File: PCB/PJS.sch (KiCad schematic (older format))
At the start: 22 parts

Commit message: Current Schematic and Footprints.
Pins between schematic and footprint are now mostly in alignment. The altimeter has a footprint, and JST connectors are to size.
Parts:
- removed S? (x4): LimitSwitch, PJS:LimitSwitch, symbol PJS:LimitSwitch
- removed X?: XT30-F_MotorConnector, PJS:XT30_Female_MotorConnector, symbol PJS:XT30-F_MotorConnector
- added S? (x7): JST_2Pin, symbol PJS:JST_2Pin
- added X? (x2): XT30-F_MotorConnector, PJS:XT30_Female_MotorConnector, symbol PJS:XT30-F_MotorConnector
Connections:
- net labels added: Door_BridgeAOut1, Door_BridgeAOut2, Door_DriverBOut1, Door_DriverBOut2, Door_RelayOut1, Door_RelayOut2, Link_DriverInA, Link_DriverInB, Link_DriverOutA, Link_DriverOutB, Link_DriverPWM, Relay_Signal
- net labels removed: LinkDriver_InA, LinkDriver_InB, LinkDriver_OutA, LinkDriver_OutB, LinkDriver_PWM, RelaySignal
- wire segments 68 -> 76
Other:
- moved on the sheet: C?, R?, X?

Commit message: 99% Complete Schematic and Footprints.
The only items on the schematic that are not complete are the switches, as the 5th switch needs to be defined and all of them should be renamed.

Some of the Teensy pins are not named properly either. Besides that, every component should be correctly associated with an accurate footprint.
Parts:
- removed A?: BMP388_AdafruitAltimeter, PJS:BMP388, symbol PJS:BMP388_AdafruitAltimeter
- removed A?: DRV8871_AuxMotorDriver, symbol PJS:DRV8871_AuxMotorDriver
- removed Q?: 2N2222_Transistor, symbol PJS:2N2222_Transistor
- removed X?: XT30-F_MotorConnector, PJS:XT30_Female_MotorConnector, symbol PJS:XT30-F_MotorConnector
- added A?: BMP388_Altimeter, PJS:BMP388_Altimeter, symbol PJS:BMP388_Altimeter
- added A? (x4): DRV8871_MotorDriver, PJS:DRV8871_MotorDriver, symbol PJS:DRV8871_MotorDriver
- added C? (x3): 47uF, PJS:EEE-1CA470SP_Capacitor, symbol PJS:CP
- added C? (x3): 0.1uF, PJS:CL05B104KO5NNNC_Capacitor, symbol PJS:C
- added Q?: MMBT222A_Transistor, PJS:MMBT2222A_Transistor, symbol PJS:MMBT222A_Transistor
- added R?: 30k, PJS:0402_Resistor, symbol PJS:R
- added R? (x2): 82k, PJS:0402_Resistor, symbol PJS:R
- added S?: JST_2Pin, symbol PJS:JST_2Pin
- added S?: JST_2Pin, PJS:JST_2Pin, symbol PJS:JST_2Pin
- A?: footprint PJS:TBS_Crossfire_RX -> PJS:TBS_Crossfire_RF_Receiver
- C?: footprint (none) -> PJS:EEE-1CA470SP_Capacitor
- C?: footprint (none) -> PJS:CL05B104KO5NNNC_Capacitor
- D?: footprint (none) -> PJS:1SS351-TB-E_Diode
- R?: footprint (none) -> PJS:0402_Resistor
- R?: footprint (none) -> PJS:MicroSD_Slot
- S? (x3): footprint (none) -> PJS:JST_2Pin
- VR?: footprint PJS:D24V22F5 -> PJS:D24V22F5_VoltageRegulator
- XM?: footprint PJS:microSD_HC_Molex_104031-0811 -> PJS:MicroSD_Slot
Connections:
- net labels added: Link_DriverIN1, Link_DriverIN2, Link_DriverOUT1, Link_DriverOUT2, LockA_DriverIN1, LockA_DriverIN2, LockA_DriverOUT1, LockA_DriverOUT2, LockA_DriverOut2, LockB_DriverIN1, LockB_DriverIN2, LockB_DriverOUT1, LockB_DriverOUT2, S3_UAS
- net labels removed: Door_BridgeAOut1, Door_BridgeAOut2, Door_DriverBOut1, Door_DriverBOut2
- wire segments 76 -> 109
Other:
- moved on the sheet: C?, D?, K?, R?, S?, X?

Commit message: library localization fixes
confuses library paths and missing files solved by including them within the realm of the github folder instead of local documents
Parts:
- A?: symbol PJS:Teensy4.0 -> PJS-rescue:Teensy4.0-PJS
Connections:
- net +5V: now also A?.~ (VUSB); no longer A?.T_VIN (VIN)
- net GND: no longer A?.GND
- net S3_UAS: now also A?.1 (1_TX1_CTX2_MISO1)
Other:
- moved on the sheet: BT?, J?, VR?, X?, XM?
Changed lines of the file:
@@
 L power:GND #PWR?
 U 1 1 5FF2ED77
-P 14200 2900
-F 0 "#PWR?" H 14200 2650 50  0001 C CNN
-F 1 "GND" V 14205 2772 50  0000 R CNN
-F 2 "" H 14200 2900 50  0001 C CNN
-F 3 "" H 14200 2900 50  0001 C CNN
-	1    14200 2900
+P 13800 2500
+F 0 "#PWR?" H 13800 2250 50  0001 C CNN
+F 1 "GND" V 13805 2372 50  0000 R CNN
+F 2 "" H 13800 2500 50  0001 C CNN
+F 3 "" H 13800 2500 50  0001 C CNN
+	1    13800 2500
 	0    1    1    0
 $EndComp
@@
 L power:+12V #PWR?
 U 1 1 5FF717BB
-P 12400 2200
-F 0 "#PWR?" H 12400 2050 50  0001 C CNN
-F 1 "+12V" V 12415 2328 50  0000 L CNN
-F 2 "" H 12400 2200 50  0001 C CNN
-F 3 "" H 12400 2200 50  0001 C CNN
-	1    12400 2200
+P 12000 1800
+F 0 "#PWR?" H 12000 1650 50  0001 C CNN
+F 1 "+12V" V 12015 1928 50  0000 L CNN
+F 2 "" H 12000 1800 50  0001 C CNN
+F 3 "" H 12000 1800 50  0001 C CNN
+	1    12000 1800
 	0    -1   -1   0
 $EndComp
@@
 L power:GND #PWR?
 U 1 1 5FF70E20
-P 13100 2150
-F 0 "#PWR?" H 13100 1900 50  0001 C CNN
-F 1 "GND" V 13105 2022 50  0000 R CNN
-F 2 "" H 13100 2150 50  0001 C CNN
-F 3 "" H 13100 2150 50  0001 C CNN
-	1    13100 2150
+P 12700 1750
+F 0 "#PWR?" H 12700 1500 50  0001 C CNN
+F 1 "GND" V 12705 1622 50  0000 R CNN
+F 2 "" H 12700 1750 50  0001 C CNN
+F 3 "" H 12700 1750 50  0001 C CNN
+	1    12700 1750
 	0    -1   -1   0
 $EndComp
@@
 L power:+5V #PWR?
 U 1 1 5FF7064D
-P 13100 2050
-F 0 "#PWR?" H 13100 1900 50  0001 C CNN
-F 1 "+5V" V 13115 2178 50  0000 L CNN
-F 2 "" H 13100 2050 50  0001 C CNN
-F 3 "" H 13100 2050 50  0001 C CNN
-	1    13100 2050
-	0    1    1    0
-$EndComp
-Text Label 13700 2700 0    50   ~ 0
+P 12700 1650
+F 0 "#PWR?" H 12700 1500 50  0001 C CNN
+F 1 "+5V" V 12715 1778 50  0000 L CNN
+F 2 "" H 12700 1650 50  0001 C CNN
+F 3 "" H 12700 1650 50  0001 C CNN
+	1    12700 1650
+	0    1    1    0
+$EndComp
+Text Label 13300 2300 0    50   ~ 0
 3.3V_Coin
 Wire Wire Line
-	14200 2700 13700 2700
+	13800 2300 13300 2300
 $Comp
 L power:GND #PWR?
 U 1 1 5FF2647A
-P 14100 2150
-F 0 "#PWR?" H 14100 1900 50  0001 C CNN
-F 1 "GND" V 14105 2022 50  0000 R CNN
-F 2 "" H 14100 2150 50  0001 C CNN
-F 3 "" H 14100 2150 50  0001 C CNN
-	1    14100 2150
+P 13700 1750
+F 0 "#PWR?" H 13700 1500 50  0001 C CNN
+F 1 "GND" V 13705 1622 50  0000 R CNN
+F 2 "" H 13700 1750 50  0001 C CNN
+F 3 "" H 13700 1750 50  0001 C CNN
+	1    13700 1750
 	0    1    1    0
 $EndComp
@@
 L power:+12V #PWR?
 U 1 1 5FF25ABF
-P 14100 2050
-F 0 "#PWR?" H 14100 1900 50  0001 C CNN
-F 1 "+12V" V 14115 2178 50  0000 L CNN
-F 2 "" H 14100 2050 50  0001 C CNN
-F 3 "" H 14100 2050 50  0001 C CNN
-	1    14100 2050
+P 13700 1650
+F 0 "#PWR?" H 13700 1500 50  0001 C CNN
+F 1 "+12V" V 13715 1778 50  0000 L CNN
+F 2 "" H 13700 1650 50  0001 C CNN
+F 3 "" H 13700 1650 50  0001 C CNN
+	1    13700 1650
 	0    -1   -1   0
 $EndComp
@@
 L PJS:XT60-F_BatteryConnector X?
 U 1 1 5FF22EAF
-P 14400 2100
-F 0 "X?" H 14400 2415 50  0000 C CNN
-F 1 "XT60-F_BatteryConnector" H 14400 2324 50  0000 C CNN
-F 2 "PJS:XT60_FemaleBatteryConnector" H 14400 2600 50  0001 C CNN
-F 3 "" H 14400 2600 50  0001 C CNN
-	1    14400 2100
+P 14000 1700
+F 0 "X?" H 14000 2015 50  0000 C CNN
+F 1 "XT60-F_BatteryConnector" H 14000 1924 50  0000 C CNN
+F 2 "PJS:XT60_FemaleBatteryConnector" H 14000 2200 50  0001 C CNN
+F 3 "" H 14000 2200 50  0001 C CNN
+	1    14000 1700
 	1    0    0    -1
 $EndComp
@@
 L PJS:36-3034-ND_CoinCellHolder BT?
 U 1 1 5FCA2E08
-P 14450 2800
-F 0 "BT?" H 14628 2846 50  0000 L CNN
-F 1 "36-3034-ND_CoinCellHolder" H 14628 2755 50  0000 L CNN
-F 2 "PJS:36-3034-ND_CoinCellHolder" H 14450 3100 50  0001 C CNN
-F 3 "" H 14450 3100 50  0001 C CNN
-	1    14450 2800
+P 14050 2400
+F 0 "BT?" H 14228 2446 50  0000 L CNN
+F 1 "36-3034-ND_CoinCellHolder" H 14228 2355 50  0000 L CNN
+F 2 "PJS:36-3034-ND_CoinCellHolder" H 14050 2700 50  0001 C CNN
+F 3 "" H 14050 2700 50  0001 C CNN
+	1    14050 2400
 	1    0    0    -1
 $EndComp
@@
 L PJS:D24V22F5_VoltageRegulator VR?
 U 1 1 5FCA09BF
-P 12750 2100
-F 0 "VR?" H 12750 2465 50  0000 C CNN
-F 1 "D24V22F5_VoltageRegulator" H 12750 2374 50  0000 C CNN
-F 2 "PJS:D24V22F5_VoltageRegulator" H 12700 1800 50  0001 C CNN
-F 3 "" H 12700 1800 50  0001 C CNN
-	1    12750 2100
+P 12350 1700
+F 0 "VR?" H 12350 2065 50  0000 C CNN
+F 1 "D24V22F5_VoltageRegulator" H 12350 1974 50  0000 C CNN
+F 2 "PJS:D24V22F5_VoltageRegulator" H 12300 1400 50  0001 C CNN
+F 3 "" H 12300 1400 50  0001 C CNN
+	1    12350 1700
 	1    0    0    -1
 $EndComp
@@
 L power:GND #PWR?
 U 1 1 5FF33FF2
-P 13100 6650
-F 0 "#PWR?" H 13100 6400 50  0001 C CNN
-F 1 "GND" V 13105 6522 50  0000 R CNN
-F 2 "" H 13100 6650 50  0001 C CNN
-F 3 "" H 13100 6650 50  0001 C CNN
-	1    13100 6650
+P 11550 7600
+F 0 "#PWR?" H 11550 7350 50  0001 C CNN
+F 1 "GND" V 11555 7472 50  0000 R CNN
+F 2 "" H 11550 7600 50  0001 C CNN
+F 3 "" H 11550 7600 50  0001 C CNN
+	1    11550 7600
 	0    1    1    0
 $EndComp
@@
 L power:GND #PWR?
 U 1 1 5FF32F5C
-P 12100 7250
-F 0 "#PWR?" H 12100 7000 50  0001 C CNN
-F 1 "GND" V 12105 7122 50  0000 R CNN
-F 2 "" H 12100 7250 50  0001 C CNN
-F 3 "" H 12100 7250 50  0001 C CNN
-	1    12100 7250
+P 10550 8200
+F 0 "#PWR?" H 10550 7950 50  0001 C CNN
+F 1 "GND" V 10555 8072 50  0000 R CNN
+F 2 "" H 10550 8200 50  0001 C CNN
+F 3 "" H 10550 8200 50  0001 C CNN
+	1    10550 8200
 	0    1    1    0
 $EndComp
@@
 L PJS:HFW8R-1STE1H1LF_FFC J?
 U 1 1 5FC972AB
-P 12500 7100
-F 0 "J?" H 12500 7715 50  0000 C CNN
-F 1 "HFW8R-1STE1H1LF_FFC" H 12500 7624 50  0000 C CNN
-F 2 "PJS:HFW8R-1STE1H1LF_FFC" H 12550 6550 50  0001 C CNN
-F 3 "" H 12550 6550 50  0001 C CNN
-	1    12500 7100
-	1    0    0    -1
-$EndComp
-Wire Wire Line
-	12100 7150 11700 7150
-Text Label 11700 7150 0    50   ~ 0
+P 10950 8050
+F 0 "J?" H 10950 8665 50  0000 C CNN
+F 1 "HFW8R-1STE1H1LF_FFC" H 10950 8574 50  0000 C CNN
+F 2 "PJS:HFW8R-1STE1H1LF_FFC" H 11000 7500 50  0001 C CNN
+F 3 "" H 11000 7500 50  0001 C CNN
+	1    10950 8050
+	1    0    0    -1
+$EndComp
+Wire Wire Line
+	10550 8100 10150 8100
+Text Label 10150 8100 0    50   ~ 0
 SD_CLK
 Wire Wire Line
-	12100 6750 11700 6750
-Wire Wire Line
-	12100 6850 11700 6850
-Text Label 11700 6750 0    50   ~ 0
+	10550 7700 10150 7700
+Wire Wire Line
+	10550 7800 10150 7800
+Text Label 10150 7700 0    50   ~ 0
 SD_DAT2
-Text Label 11700 6850 0    50   ~ 0
+Text Label 10150 7800 0    50   ~ 0
 SD_DAT3
-Text Label 11700 6950 0    50   ~ 0
+Text Label 10150 7900 0    50   ~ 0
 SD_CMD
 Wire Wire Line
-	12100 6950 11700 6950
-Text Label 11700 7050 0    50   ~ 0
+	10550 7900 10150 7900
+Text Label 10150 8000 0    50   ~ 0
 SD_VDD
 Wire Wire Line
-	11700 7050 12100 7050
-Text Label 11700 7350 0    50   ~ 0
+	10150 8000 10550 8000
+Text Label 10150 8300 0    50   ~ 0
 SD_DAT0
 Wire Wire Line
-	12100 7350 11700 7350
-Text Label 11700 7450 0    50   ~ 0
+	10550 8300 10150 8300
+Text Label 10150 8400 0    50   ~ 0
 SD_DAT1
 Wire Wire Line
-	12100 7450 11700 7450
-Wire Wire Line
-	12900 6750 13100 6750
-Wire Wire Line
-	12900 6850 13100 6850
-Wire Wire Line
-	12900 6950 13100 6950
-Wire Wire Line
-	12900 7050 13100 7050
-Wire Wire Line
-	12900 7150 13100 7150
-Wire Wire Line
-	12900 7250 13100 7250
-Wire Wire Line
-	12900 7350 13100 7350
-Wire Wire Line
-	12900 7450 13100 7450
+	10550 8400 10150 8400
+Wire Wire Line
+	11350 7700 11550 7700
+Wire Wire Line
+	11350 7800 11550 7800
+Wire Wire Line
+	11350 7900 11550 7900
+Wire Wire Line
+	11350 8000 11550 8000
+Wire Wire Line
+	11350 8100 11550 8100
+Wire Wire Line
+	11350 8200 11550 8200
+Wire Wire Line
+	11350 8300 11550 8300
+Wire Wire Line
+	11350 8400 11550 8400
 $Comp
 L PJS:MicroSD_Slot XM?
 U 1 1 5FC9CA50
-P 14000 7050
-F 0 "XM?" H 14630 7121 50  0000 L CNN
-F 1 "MicroSD_Slot" H 14630 7030 50  0000 L CNN
-F 2 "PJS:MicroSD_Slot" H 15150 7350 50  0001 C CNN
-F 3 "http://katalog.we-online.de/em/datasheet/693072010801.pdf" H 13800 7050 50  0001 C CNN
-	1    14000 7050
+P 12450 8000
+F 0 "XM?" H 13080 8071 50  0000 L CNN
+F 1 "MicroSD_Slot" H 13080 7980 50  0000 L CNN
+F 2 "PJS:MicroSD_Slot" H 13600 8300 50  0001 C CNN
+F 3 "http://katalog.we-online.de/em/datasheet/693072010801.pdf" H 12250 8000 50  0001 C CNN
+	1    12450 8000
 	1    0    0    -1
 $EndComp
@@
 $EndComp
 $Comp
-L PJS:Teensy4.0 A?
+L PJS-rescue:Teensy4.0-PJS A?
 U 1 1 5FC9DE2C
 P 8550 4500
@@
 Wire Wire Line
 	10100 5550 9650 5550
+Wire Wire Line
+	7450 3350 6900 3350
+Text Label 6900 3350 0    50   ~ 0
+S3_UAS
 $EndSCHEMATC

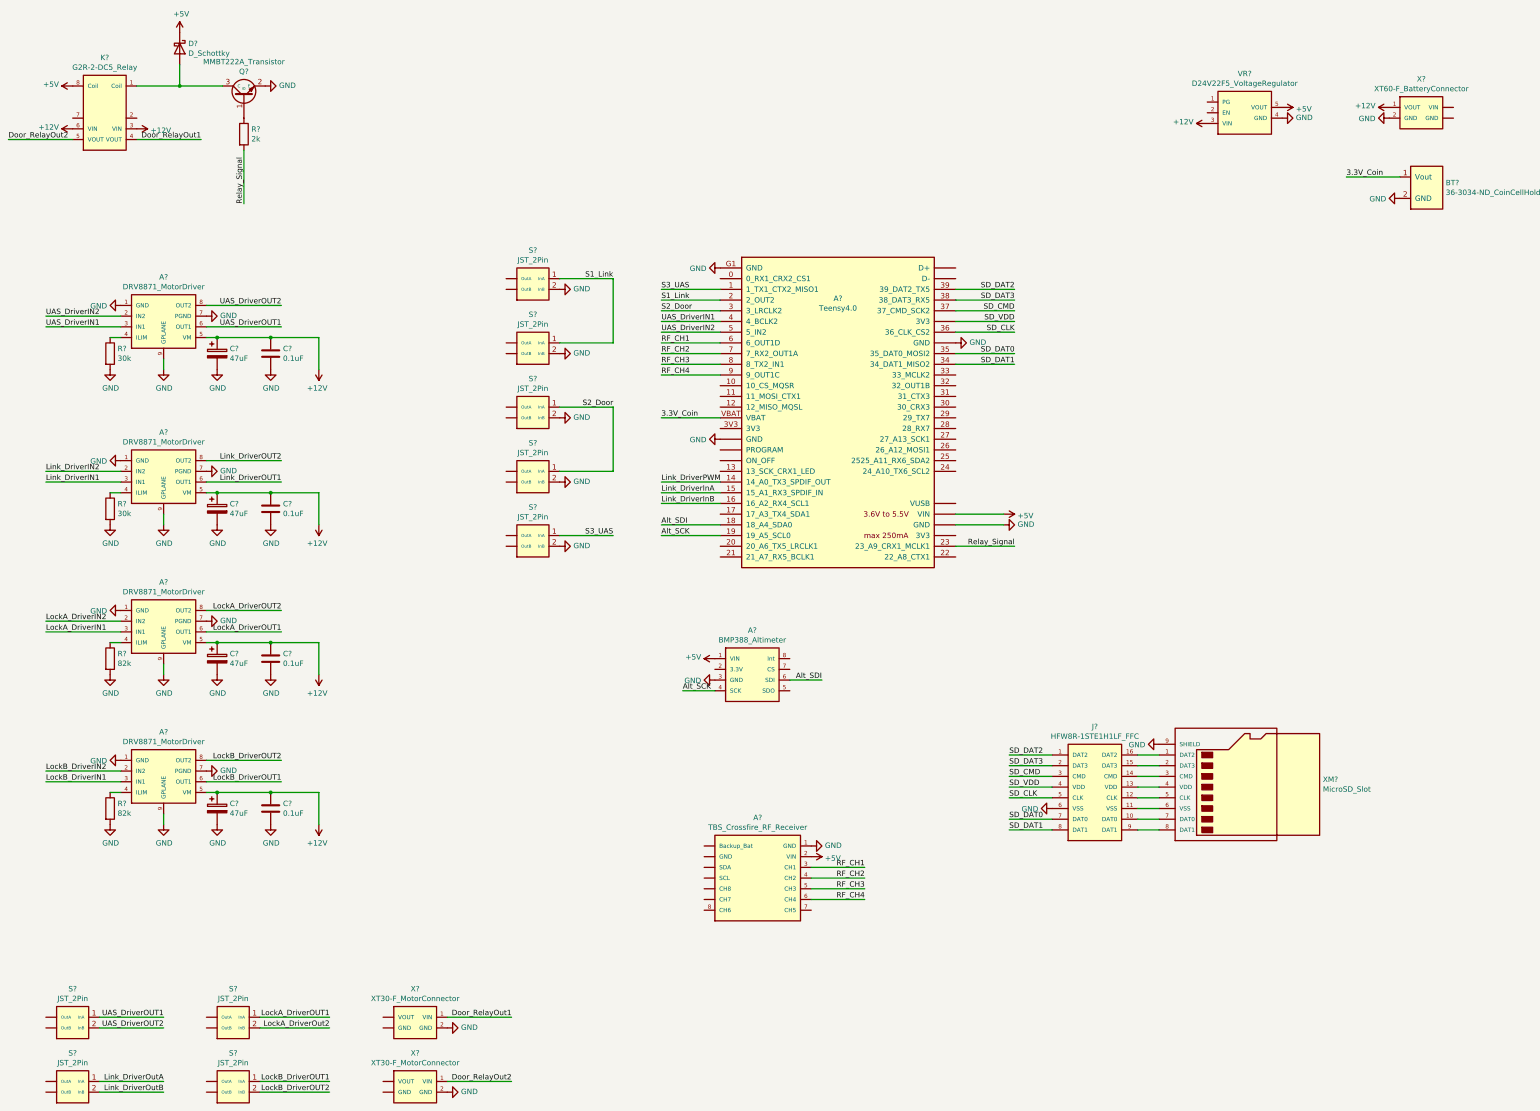
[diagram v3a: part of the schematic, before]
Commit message: teensy breakout, limit switch connection, dxf for board
added teensy breakout to schematic, and added missing limit switch connections. also inserted DXF of board dimensions to the PCB file (le monke)
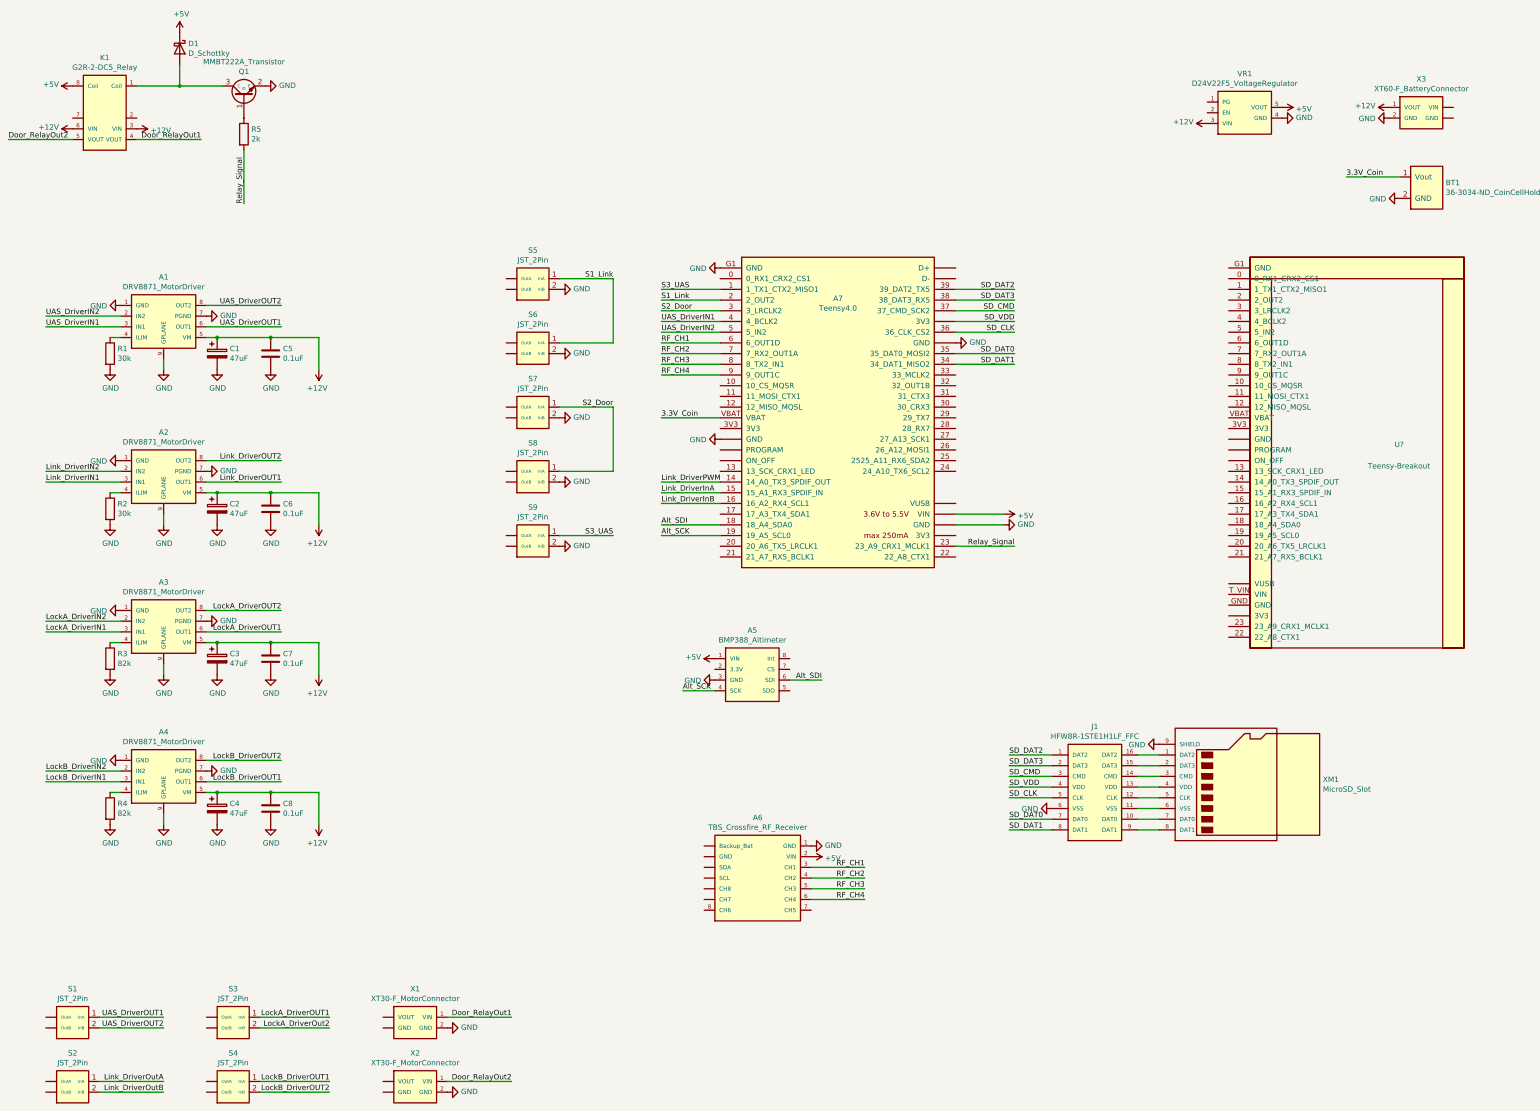
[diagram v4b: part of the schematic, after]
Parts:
- added U?: Teensy-Breakout, PJS:Teensy4.0, symbol PJS:Teensy-Breakout
- gave numbers to parts that had none: 39
